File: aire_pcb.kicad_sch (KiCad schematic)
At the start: 28 parts

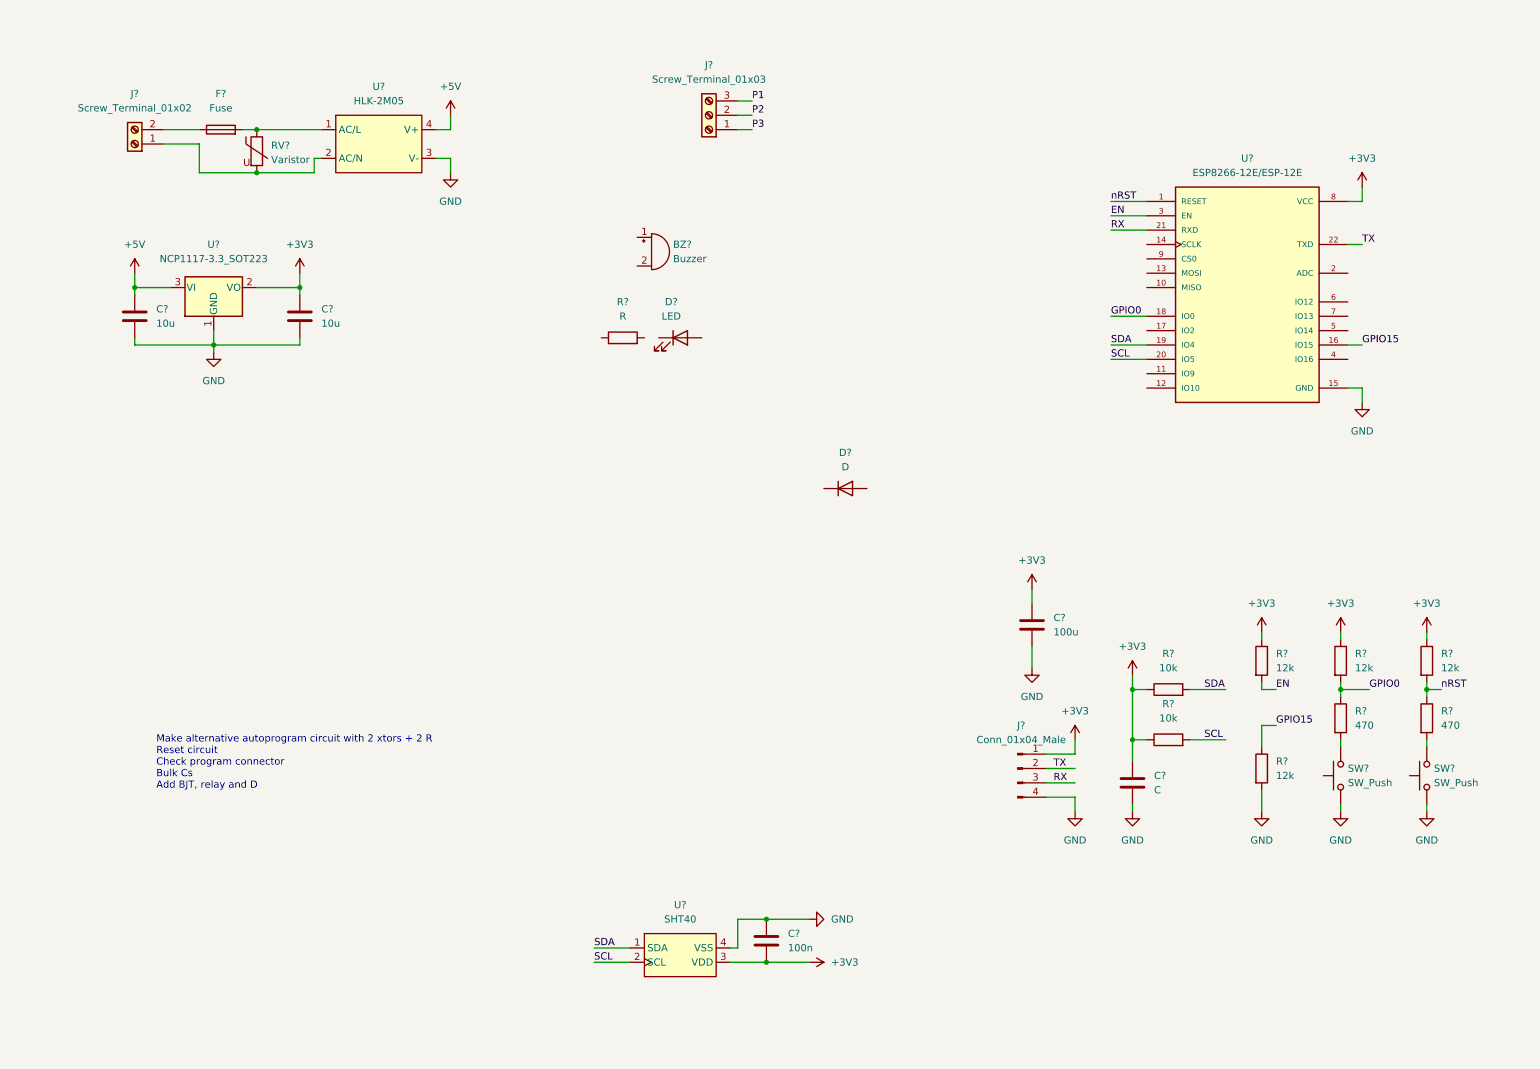
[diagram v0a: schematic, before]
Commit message: First sch version. Add all footprints and 3d models
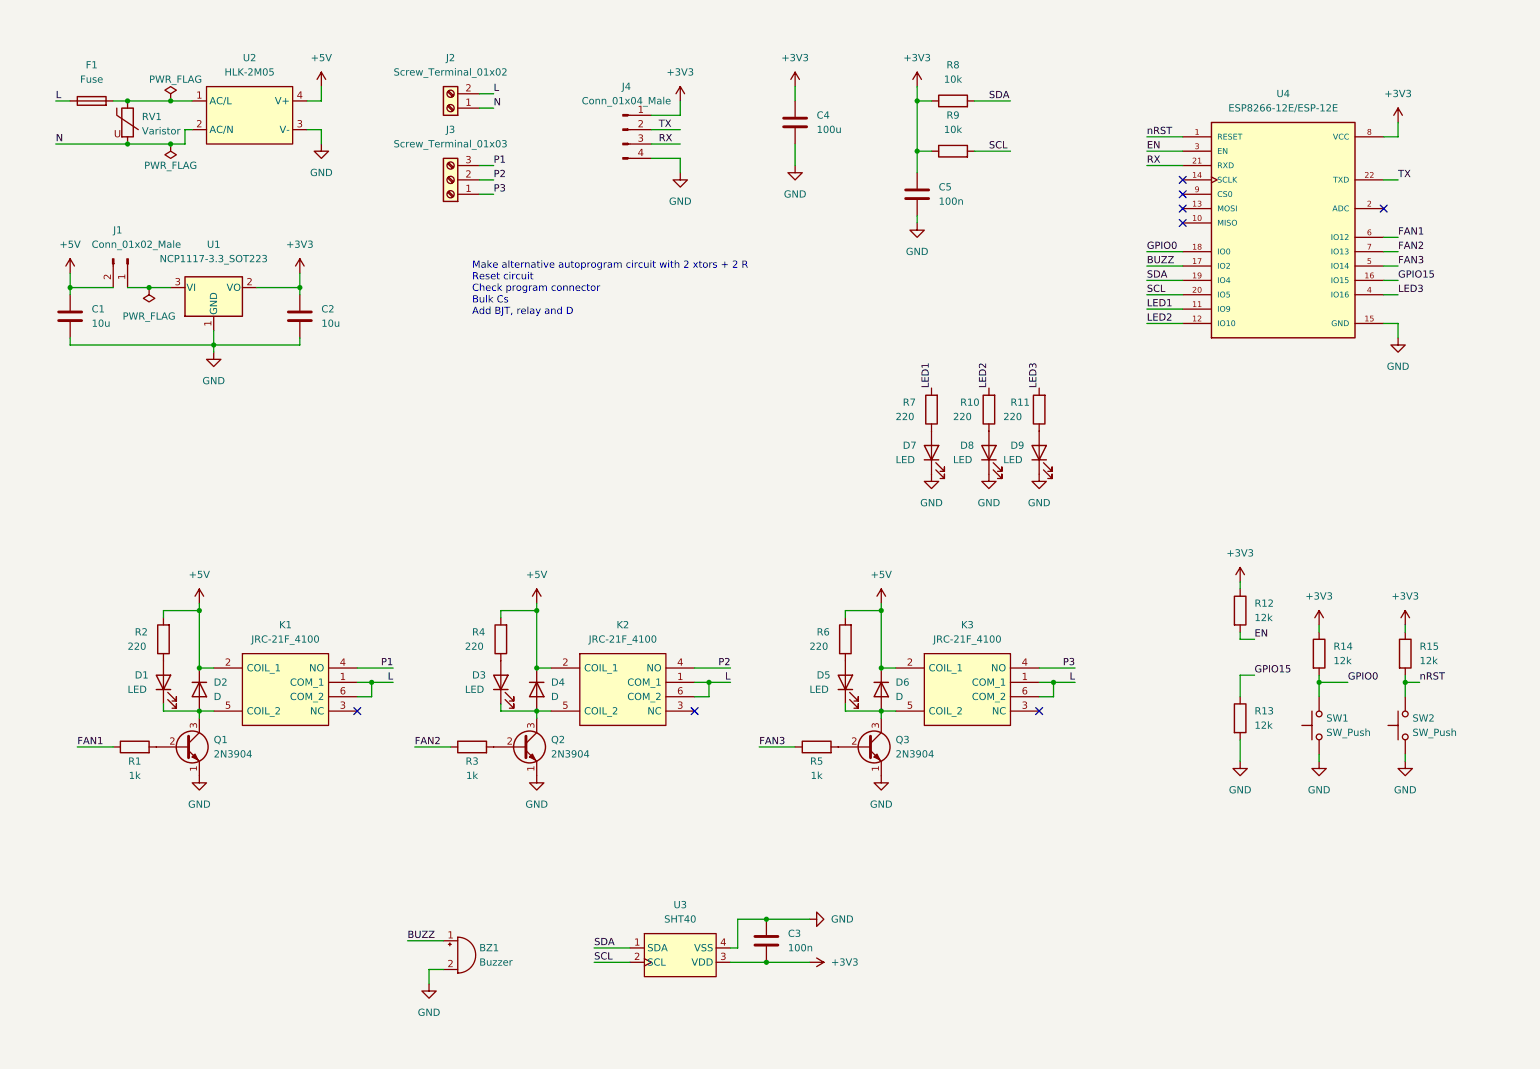
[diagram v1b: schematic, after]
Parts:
- removed R? (x2): 470, symbol Device:R
- removed U?: ESP8266-12E/ESP-12E, XCVR_ESP8266-12E/ESP-12E, symbol esp8266-12e:ESP8266-12E/ESP-12E
- added D3, D5: LED, LED_SMD:LED_0402_1005Metric, symbol Device:LED
- added D4, D6: D, Diode_THT:D_A-405_P7.62mm_Horizontal, symbol Device:D
- added D7, D8, D9: LED, LED_THT:LED_D5.0mm, symbol Device:LED
- added J1: Conn_01x02_Male, Connector_PinHeader_2.54mm:PinHeader_1x02_P2.54mm_Vertical, symbol Connector:Conn_01x02_Male
- added K1, K2, K3: JRC-21F_4100, guille_3rdparty:JRC21F4100, symbol guille_3rdparty:JRC-21F_4100
- added Q1, Q2, Q3: 2N3904, Package_TO_SOT_THT:TO-92_Inline, symbol Transistor_BJT:2N3904
- added R1, R3, R5: 1k, Resistor_SMD:R_0402_1005Metric, symbol Device:R
- added R10, R11, R4, R6, R7: 220, Resistor_SMD:R_0402_1005Metric, symbol Device:R
- added U4: ESP8266-12E/ESP-12E, guille_3rdparty:ESP8266-12E, symbol guille_3rdparty:ESP8266-12E{brace}slash}ESP-12E
- BZ1: renamed from BZ?; footprint (none) -> Buzzer_Beeper:Buzzer_12x9.5RM7.6
- C1, C2, C4: renamed from C?; footprint (none) -> Capacitor_SMD:C_1206_3216Metric
- C3: renamed from C?; footprint (none) -> Capacitor_SMD:C_0402_1005Metric
- C5: renamed from C?; value C -> 100n; footprint (none) -> Capacitor_SMD:C_0402_1005Metric
- D1: renamed from D?; footprint (none) -> LED_SMD:LED_0402_1005Metric
- D2: renamed from D?; footprint (none) -> Diode_THT:D_A-405_P7.62mm_Horizontal
- F1: renamed from F?; footprint (none) -> guille_3rdparty:Fuse_2512_6332Metric
- J2: renamed from J?; footprint (none) -> TerminalBlock_Phoenix:TerminalBlock_Phoenix_MKDS-1,5-2-5.08_1x02_P5.08mm_Horizontal
- J3: renamed from J?; footprint (none) -> TerminalBlock_Phoenix:TerminalBlock_Phoenix_MKDS-1,5-3-5.08_1x03_P5.08mm_Horizontal
- J4: renamed from J?; footprint (none) -> Connector_PinHeader_2.54mm:PinHeader_1x04_P2.54mm_Vertical
- R12, R13, R14, R15, R8, R9: renamed from R?; footprint (none) -> Resistor_SMD:R_0402_1005Metric
- R2: renamed from R?; value R -> 220; footprint (none) -> Resistor_SMD:R_0402_1005Metric
- RV1: renamed from RV?; footprint (none) -> Varistor:RV_Disc_D12mm_W3.9mm_P7.5mm
- SW1, SW2: renamed from SW?; footprint (none) -> guille_3rdparty:SW_SPST_PTS810
- U2: renamed from U?; footprint (none) -> guille_library:HLK-2M05
- U3: renamed from U?; footprint (none) -> guille_3rdparty:SHT40
- gave numbers to parts that had none: 1
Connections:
- net +3V3: now also U4.8 (VCC)
- net +5V: now also D2.1 (K), R2.2, D4.1 (K), D6.1 (K), J1.2 (Pin_2), K1.2 (COIL_1), K2.2 (COIL_1), K3.2 (COIL_1), R4.2, R6.2; no longer U1.3 (VI)
- net EN: now also U4.3 (EN)
- net GND: now also BZ1.2 (+), D7.1 (K), D8.1 (K), D9.1 (K), Q1.1 (E), Q2.1 (E), Q3.1 (E), U4.15 (GND)
- net GPIO0: now also SW1.2, U4.18 (IO0)
- net GPIO15: now also U4.16 (IO15)
- net P1: now also K1.4 (NO)
- net P2: now also K2.4 (NO)
- net P3: now also K3.4 (NO)
- net RX: now also U4.21 (RXD)
- net SCL: now also U4.20 (IO5)
- net SDA: now also U4.19 (IO4)
- net TX: now also U4.22 (TXD)
- net nRST: now also SW2.2, U4.1 (RESET)
- net N: now reaches J2.1 (Pin_1), RV1.2, U2.2 (AC/N)
- net L: now reaches F1.1, J2.2 (Pin_2)
- net L: now also K1.1 (COM_1), K1.6 (COM_2), K2.1 (COM_1), K2.6 (COM_2), K3.1 (COM_1), K3.6 (COM_2)
- net at R2.1: now also D1.2 (A)
- net at D1.1 (K): now also D2.2 (A), K1.5 (COIL_2), Q1.3 (C)
- net BUZZ: now reaches BZ1.1 (-)
- net BUZZ: now also U4.17 (IO2)
- new net: J1.1 (Pin_1), U1.3 (VI)
- new net: Q3.2 (B), R5.2
- new net: Q2.2 (B), R3.2
- new net: D3.2 (A), R4.1
- new net: D9.2 (A), R11.1
- new net: D7.2 (A), R7.1
- new net: D5.1 (K), D6.2 (A), K3.5 (COIL_2), Q3.3 (C)
- new net: D3.1 (K), D4.2 (A), K2.5 (COIL_2), Q2.3 (C)
- new net: Q1.2 (B), R1.2
- new net: D5.2 (A), R6.1
- new net: D8.2 (A), R10.1
- new net FAN1: R1.1, U4.6 (IO12)
- new net FAN2: R3.1, U4.7 (IO13)
- new net FAN3: R5.1, U4.5 (IO14)
- new net LED1: R7.2, U4.11 (IO9)
- new net LED2: R10.2, U4.12 (IO10)
- new net LED3: R11.2, U4.4 (IO16)
- no-connect marks 0 -> 8
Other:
- moved on the sheet: BZ1, C1, C4, C5, D1, D2, F1, J2, J3, J4, R12, R13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

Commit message: First placement
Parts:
- added H1, H2, H3, H4: MountingHole, MountingHole:MountingHole_3.2mm_M3_DIN965, symbol Mechanical:MountingHole
- renumbered R13 to R12, R14 to R13, R15 to R14, R12 to R15
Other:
- note added: "Add expansion port (with I2C) for display"
- note removed: "Make alternative autoprogram circuit with 2 xtors + 2 R Reset circuit Check program connector Bulk Cs Add BJT, relay and D"
- moved on the sheet: R12, R13, R14, R15, SW1, SW2

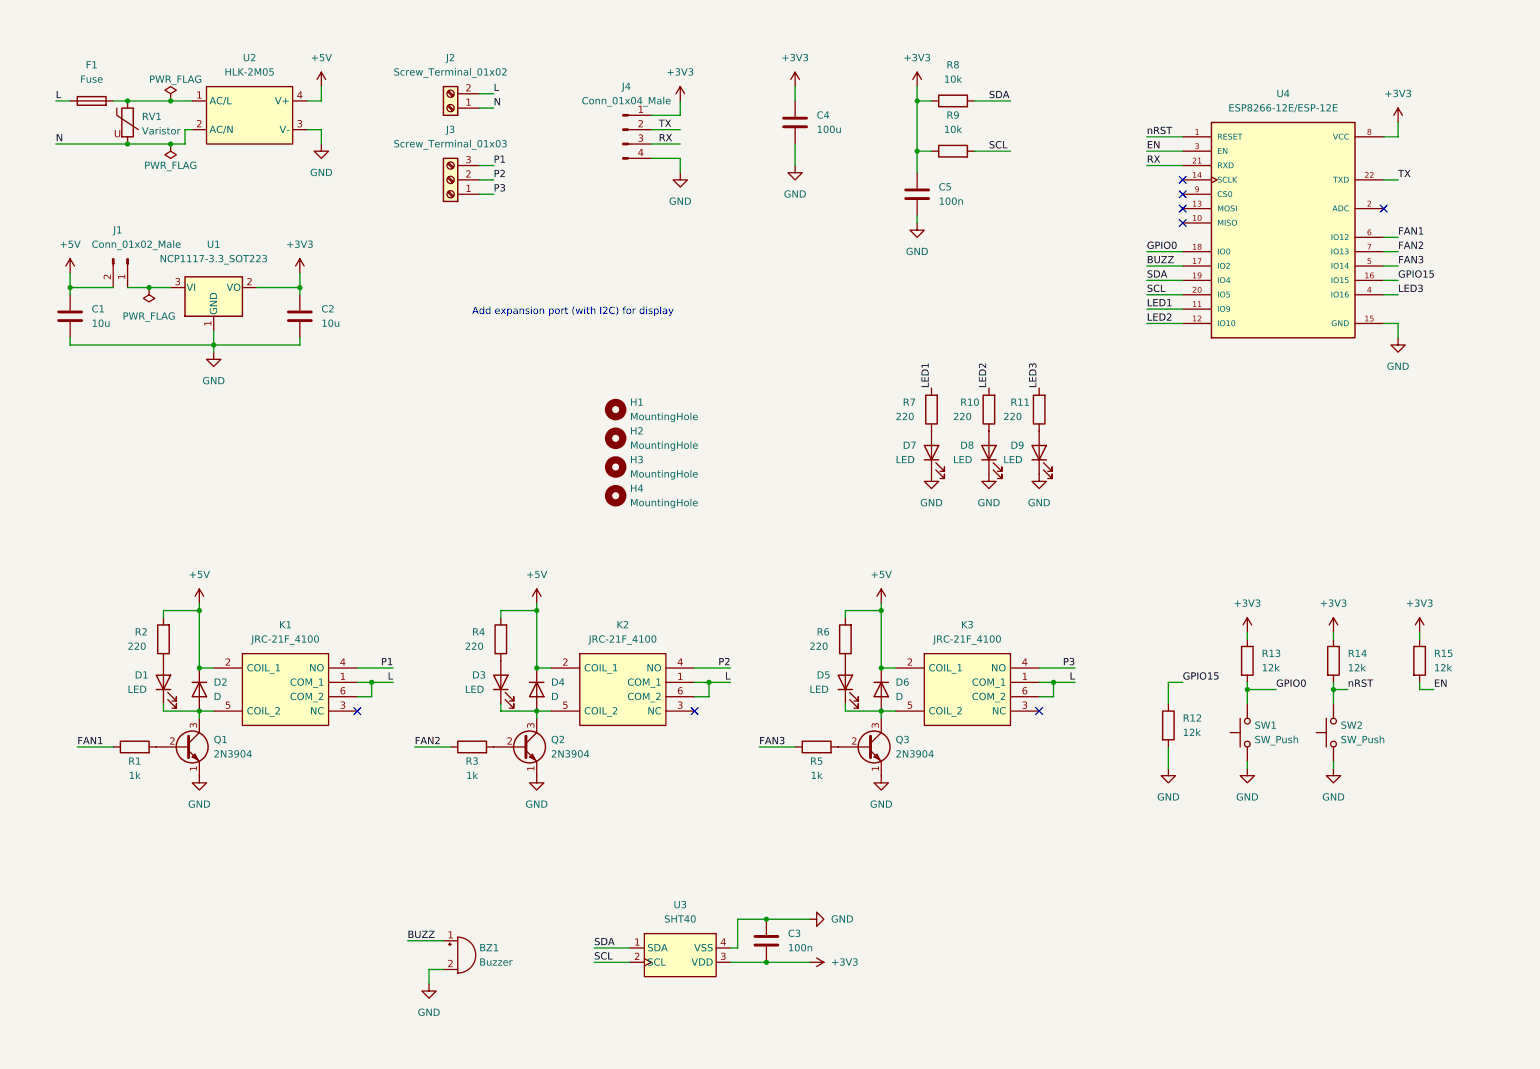
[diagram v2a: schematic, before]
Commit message: Improve placement and add expansion conenctor
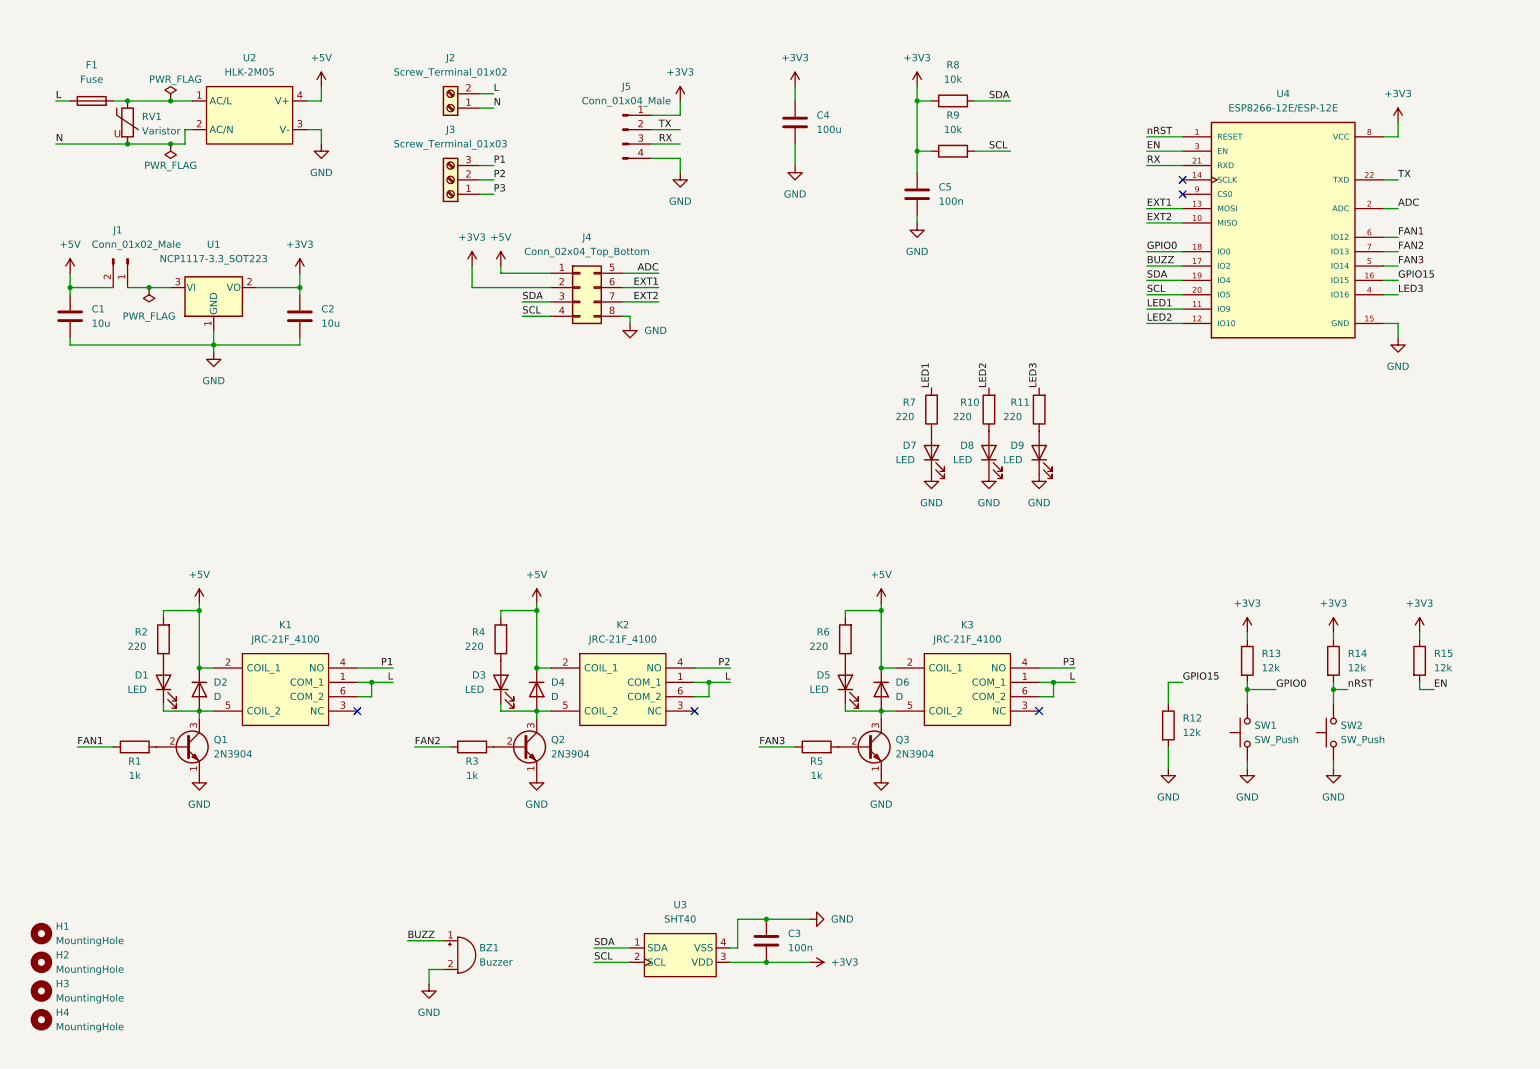
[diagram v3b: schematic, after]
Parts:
- added J4: Conn_02x04_Top_Bottom, Connector_PinHeader_2.54mm:PinHeader_2x04_P2.54mm_Vertical, symbol Connector_Generic:Conn_02x04_Top_Bottom
- D7, D8, D9: footprint LED_THT:LED_D5.0mm -> LED_THT:LED_D3.0mm
- renumbered J4 to J5
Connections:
- net +3V3: now also J4.2 (Pin_2)
- net +5V: now also J4.1 (Pin_1)
- net GND: now also J4.8 (Pin_8)
- net SCL: now also J4.4 (Pin_4)
- net SDA: now also J4.3 (Pin_3)
- net EXT2: now reaches U4.10 (MISO)
- net EXT2: now also J4.7 (Pin_7)
- net EXT1: now reaches U4.13 (MOSI)
- net EXT1: now also J4.6 (Pin_6)
- net ADC: now reaches U4.2 (ADC)
- net ADC: now also J4.5 (Pin_5)
- no-connect marks 8 -> 5
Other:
- note removed: "Add expansion port (with I2C) for display"
- moved on the sheet: H1, H2, H3, H4

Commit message: Route PCB with DRC ok
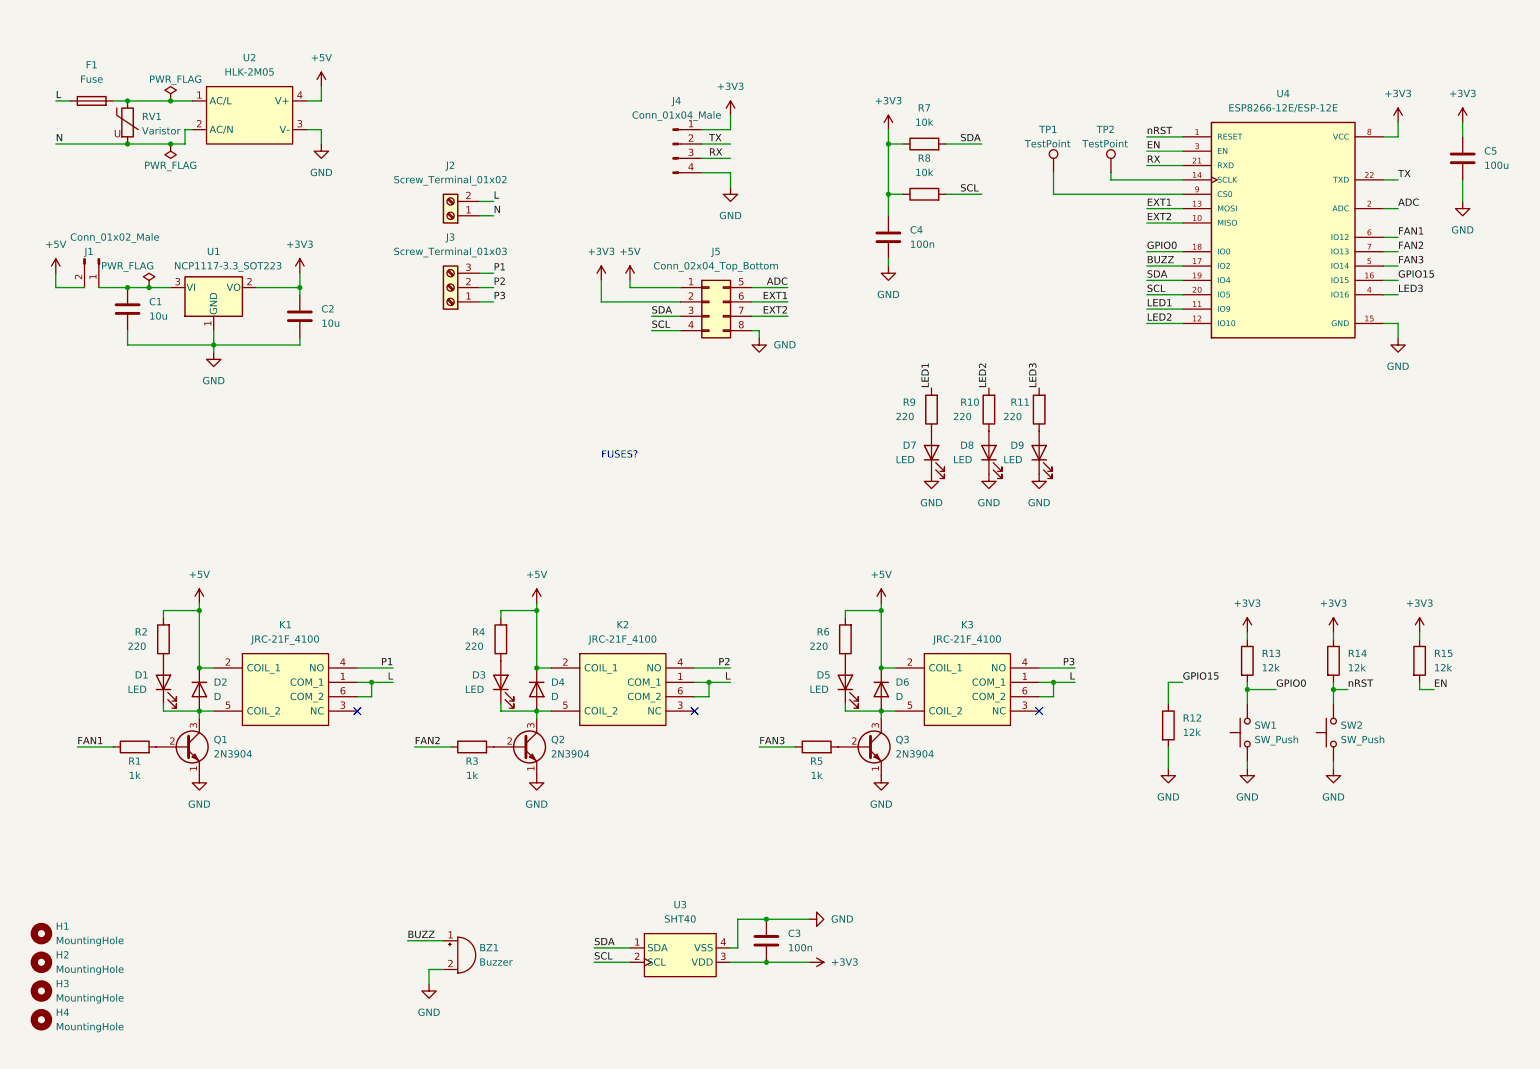
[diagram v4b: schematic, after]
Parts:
- added TP1, TP2: TestPoint, TestPoint:TestPoint_Pad_D1.5mm, symbol Connector:TestPoint
- renumbered C5 to C4, C4 to C5, J5 to J4, J4 to J5, R8 to R7, R9 to R8, R7 to R9
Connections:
- net +5V: no longer C1.1
- net at J1.1 (Pin_1), U1.3 (VI): now also C1.1
- net at U4.14 (SCLK): now also TP2.1
- net at U4.9 (CS0): now also TP1.1
- no-connect marks 5 -> 3
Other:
- note added: "FUSES?"
- moved on the sheet: C1, C4, C5, J1, J2, J3, J4, J5, R7, R8
